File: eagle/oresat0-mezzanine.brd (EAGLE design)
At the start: 80 x 71.5 mm, 29 parts, among them J1 R107064070, J10 R107064070, J2 R107064070, J3 R107064070, J4 R107064070, J5 R107064070, J6 R107064070, J7 R107064070, J8 R107064070, J9 R107064070, U1 QBA-07+, U2 QBA-07+, U3 QBA-07+, U7 QCN-19+, U8 QCN-19+, U9 QCN-19+

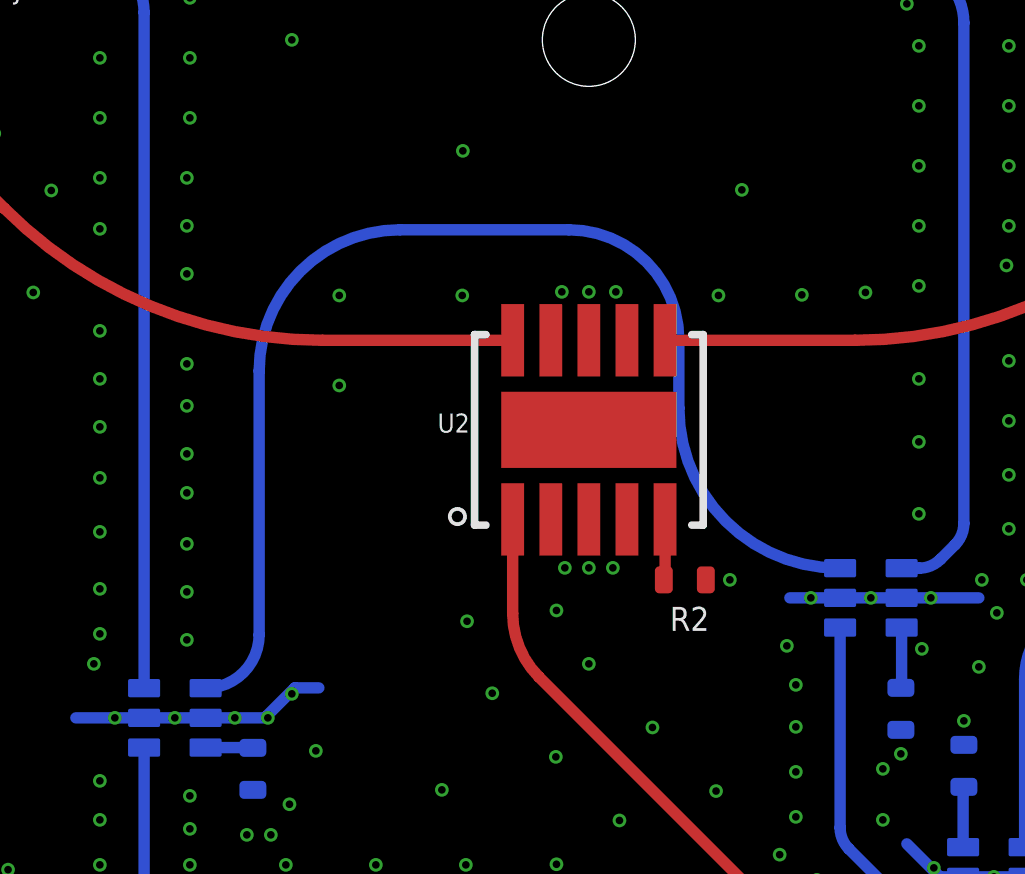
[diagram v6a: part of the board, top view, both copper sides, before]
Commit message: added vias along new short+1/4wave trace
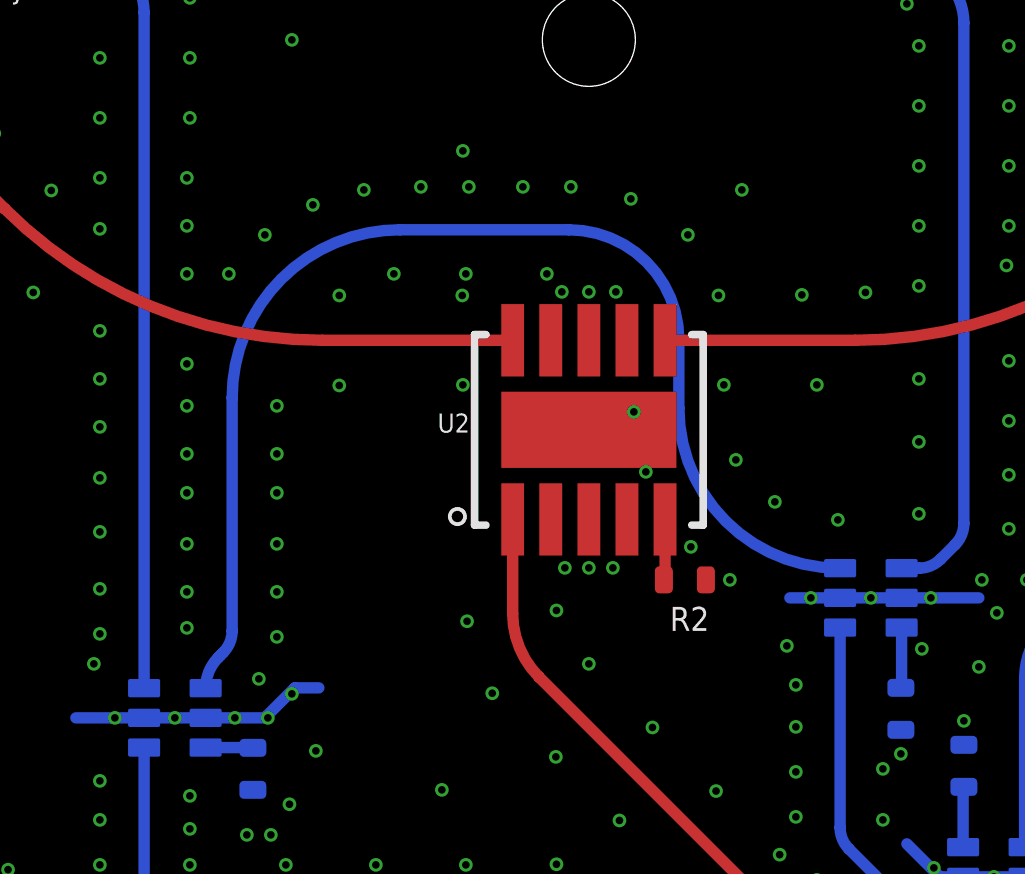
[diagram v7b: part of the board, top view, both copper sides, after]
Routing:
- net GND: vias 512 -> 541
